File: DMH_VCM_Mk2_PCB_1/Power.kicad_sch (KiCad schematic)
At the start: 13 parts, among them J100 IDC_02x05, U1 TL074, U2 TL074

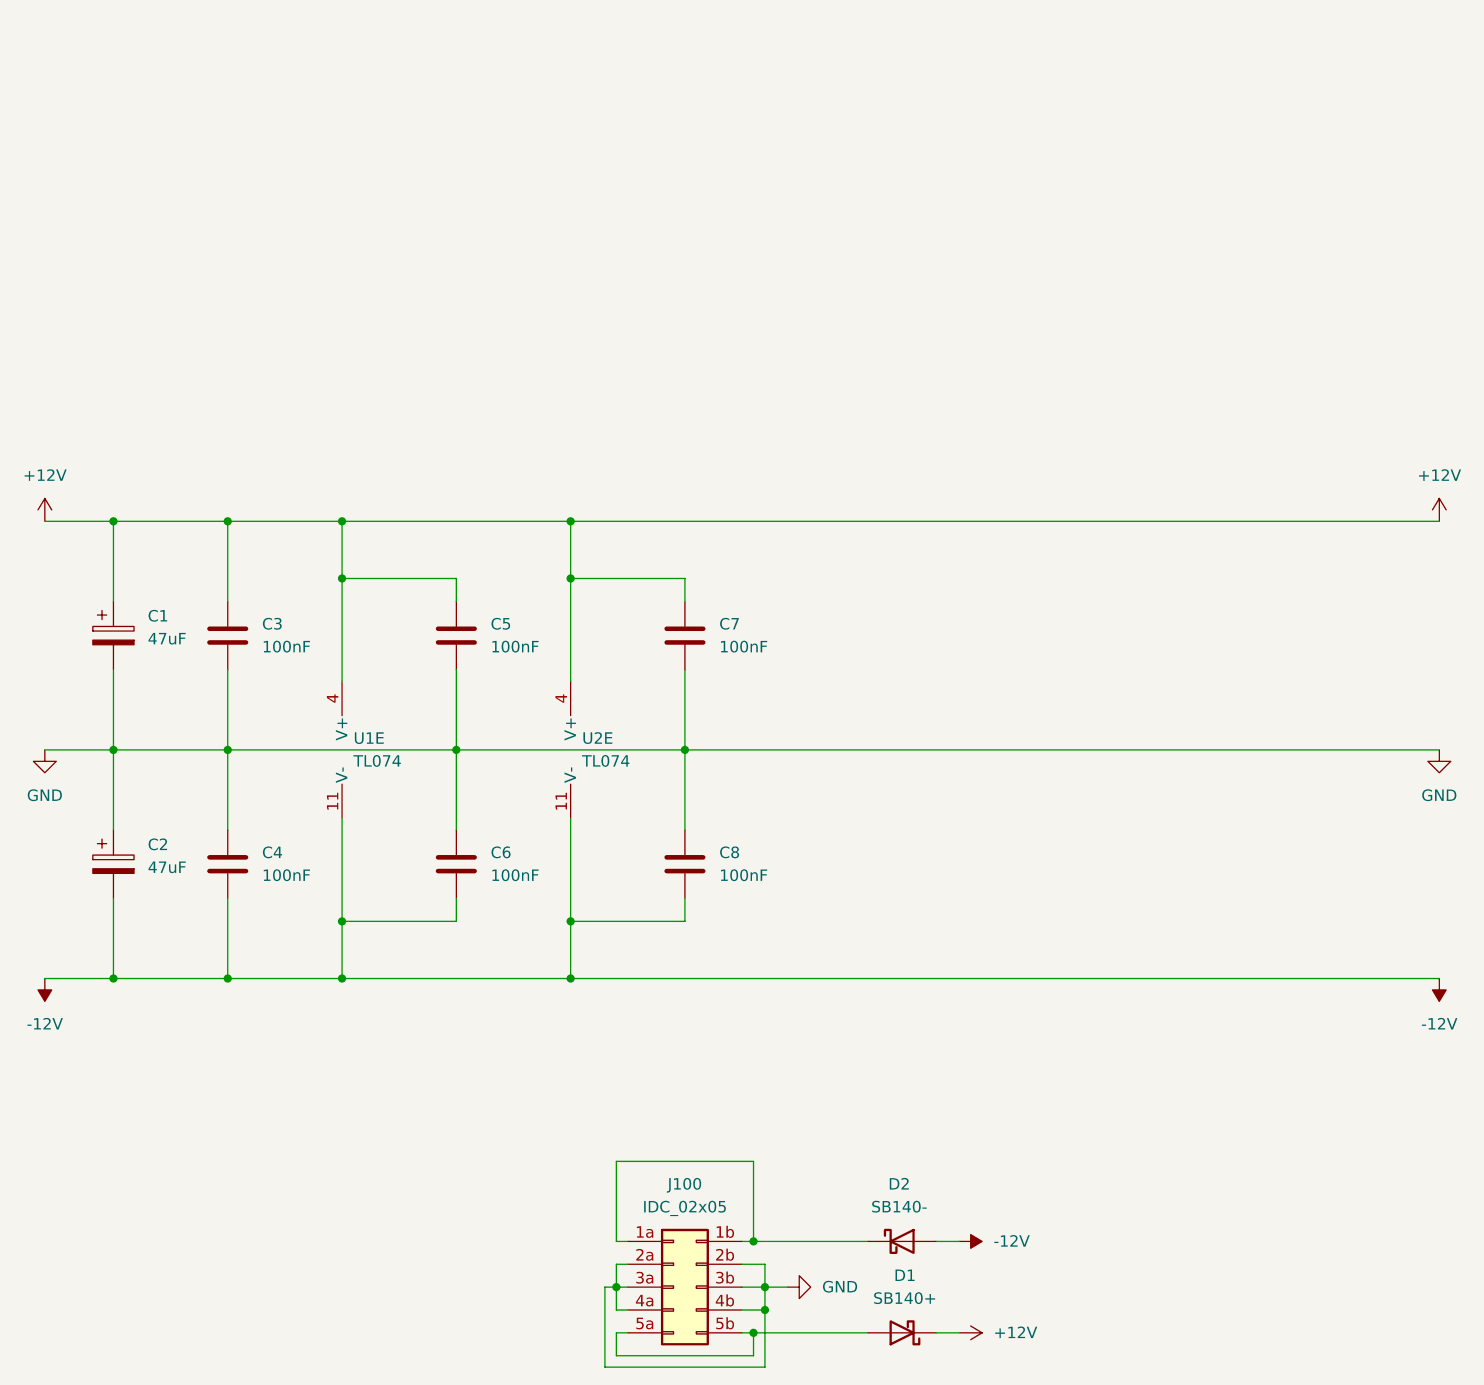
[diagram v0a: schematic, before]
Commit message: Almost finished PCB 1 schematic
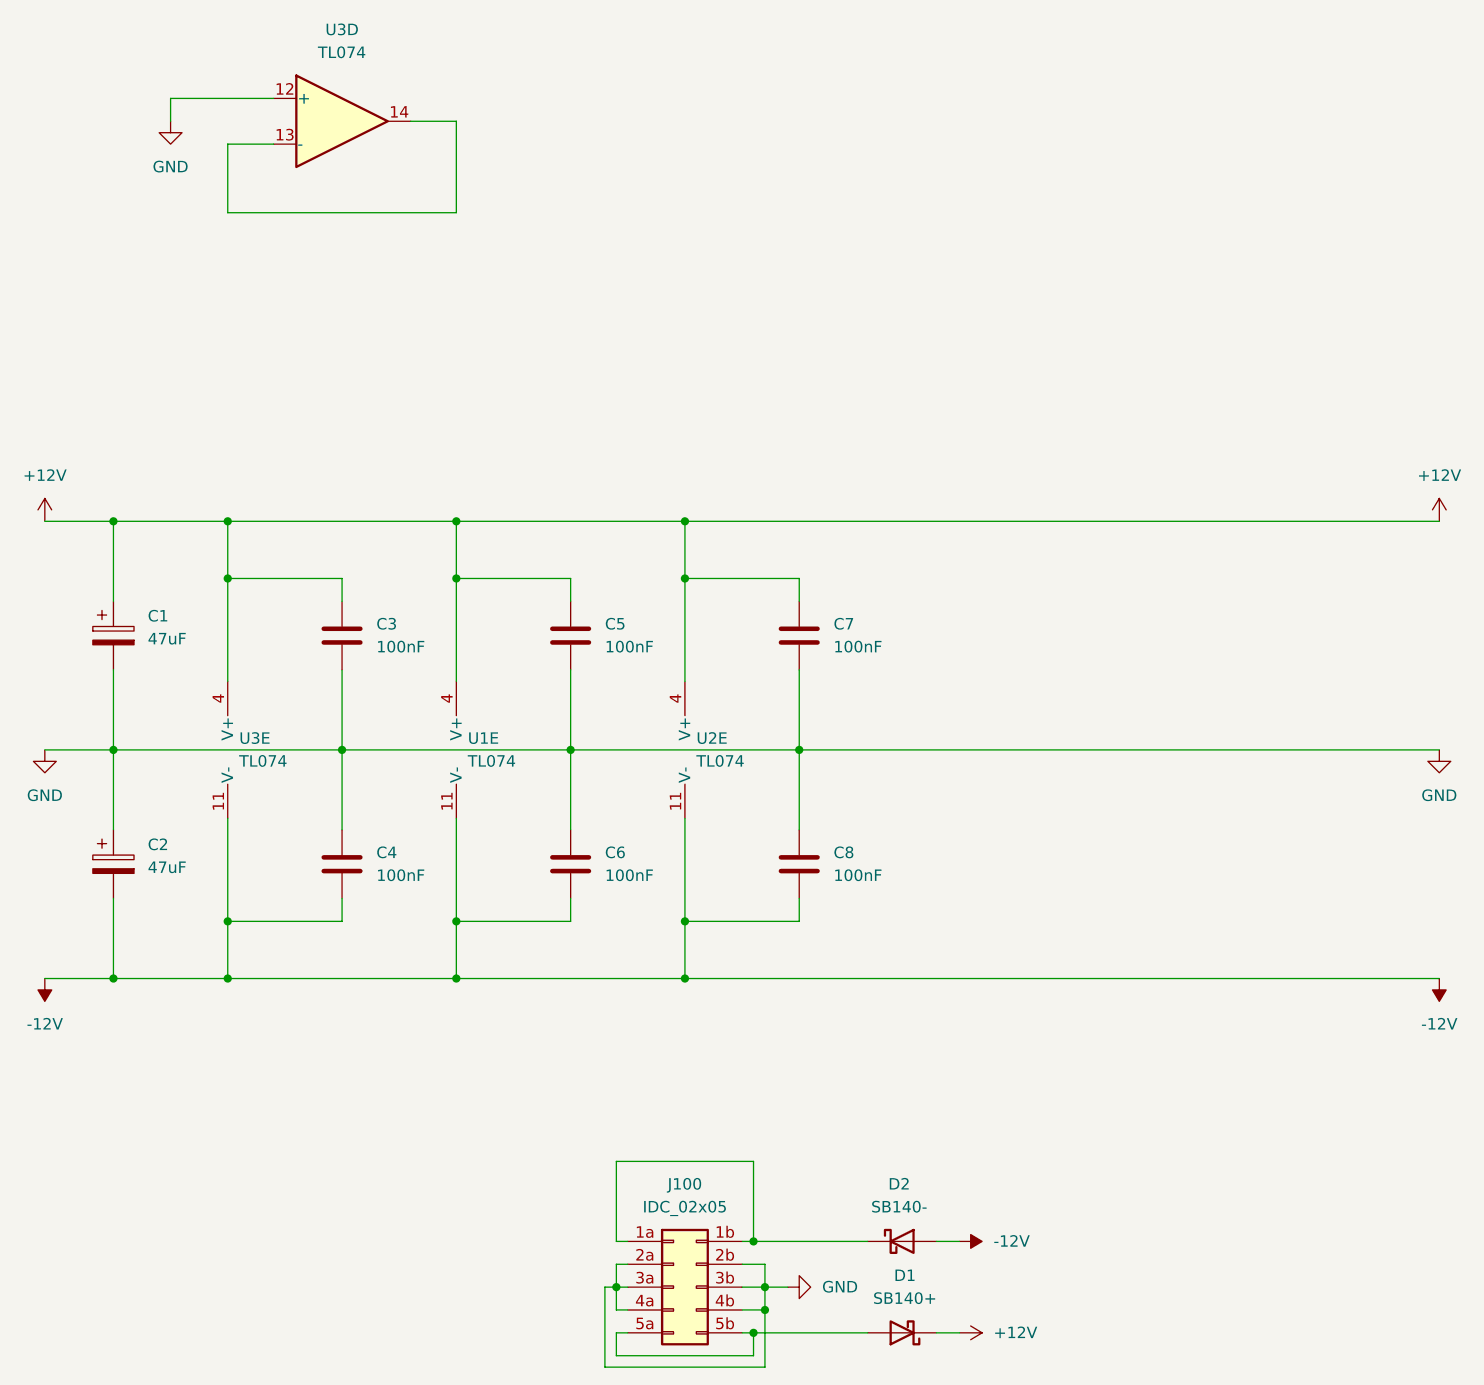
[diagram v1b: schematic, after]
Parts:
- added U3: TL074, symbol Amplifier_Operational:TL074
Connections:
- net +12V: now also U3.4 (V+)
- net -12V: now also U3.11 (V-)
- net GND: now also U3.12 (+)
- new net: U3.13 (-), U3.14
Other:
- moved on the sheet: C3, C4, C5, C6, C7, C8, U1E, U2E

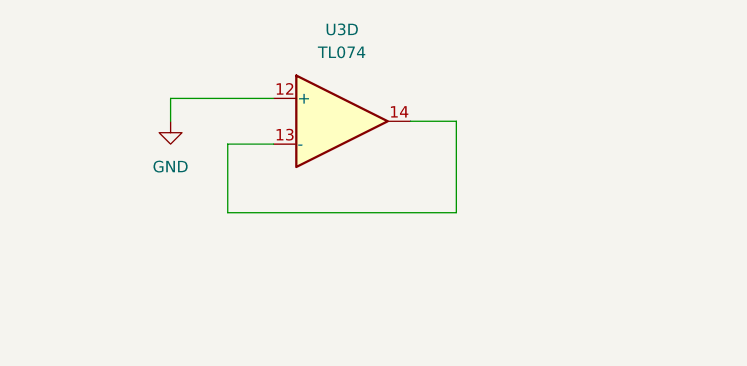
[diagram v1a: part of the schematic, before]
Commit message: PCB 1 placement in progress
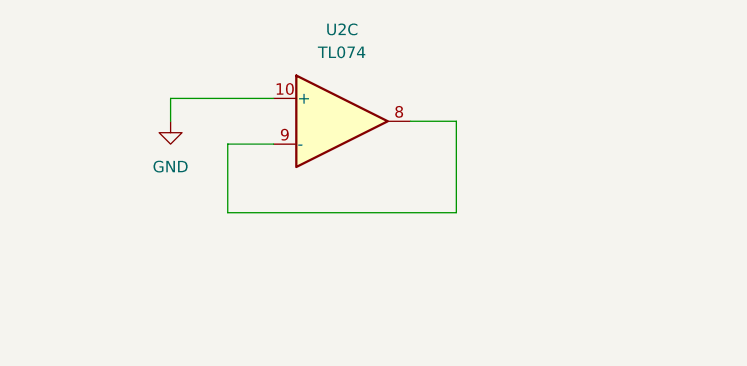
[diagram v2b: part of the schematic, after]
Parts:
- U2: renamed from U3; footprint (none) -> Package_DIP:DIP-14_W7.62mm_Socket
- U3: footprint (none) -> Package_DIP:DIP-14_W7.62mm_Socket
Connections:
- net GND: now also U2.10 (+); no longer U2.12 (+)
- new net: U2.8, U2.9 (-)
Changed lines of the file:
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@@
 		(lib_id "Amplifier_Operational:TL074")
 		(at 50.8 50.8 0)
-		(unit 4)
-		(exclude_from_sim no)
-		(in_bom yes)
-		(on_board yes)
-		(dnp no)
-		(fields_autoplaced yes)
-		(property "Reference" "U3"
+		(unit 3)
+		(exclude_from_sim no)
+		(in_bom yes)
+		(on_board yes)
+		(dnp no)
+		(fields_autoplaced yes)
+		(property "Reference" "U2"
 			(at 50.8 40.64 0)
 			(effects
@@
 			)
 		)
-		(property "Footprint" ""
+		(property "Footprint" "Package_DIP:DIP-14_W7.62mm_Socket"
 			(at 49.53 48.26 0)
 			(effects
@@
 				)
 				(hide yes)
+			)
+		)
+		(property "Function" ""
+			(at 50.8 50.8 0)
+			(effects
+				(font
+					(size 1.27 1.27)
+				)
 			)
 		)
@@
 			(project ""
 				(path "/58f4306d-5387-4983-bb08-41a2313fd315/0cdf34b2-39cd-4d9e-981a-97cd34791509"
-					(reference "U3")
-					(unit 4)
+					(reference "U2")
+					(unit 3)
 				)
 			)
@@
 			)
 		)
-		(property "Footprint" ""
+		(property "Footprint" "Package_DIP:DIP-14_W7.62mm_Socket"
 			(at 39.37 118.11 0)
 			(effects
@@
 			)
 		)
+		(property "Function" ""
+			(at 40.64 120.65 0)
+			(effects
+				(font
+					(size 1.27 1.27)
+				)
+			)
+		)

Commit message: Kicad 10 and updated SynthStuff
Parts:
- D1: value SB140+ -> SB140; symbol SynthStuff:Power_Bus_Schotty_+ -> Diode:SB140
- D2: value SB140- -> SB140; symbol SynthStuff:Power_Bus_Schotty_- -> Diode:SB140
